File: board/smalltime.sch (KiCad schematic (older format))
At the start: 60 parts, among them IC1 STM32F030K6T6, IC2 MCP1700, IC3 DS3231MZ, J1 MICROUSB, P1 SWD, P2 SWD_TC, Q1 PFET, Q10 TEPT4400, Q2 PFET, Q3 PFET, Q4 PFET, Q5 PFET, Q6 PFET, Q7 PFET, Q8 PFET, Q9 PFET, SW1 INC, SW2 SET, U1 COM-09481, U2 COM-09481, X1 BATTERY

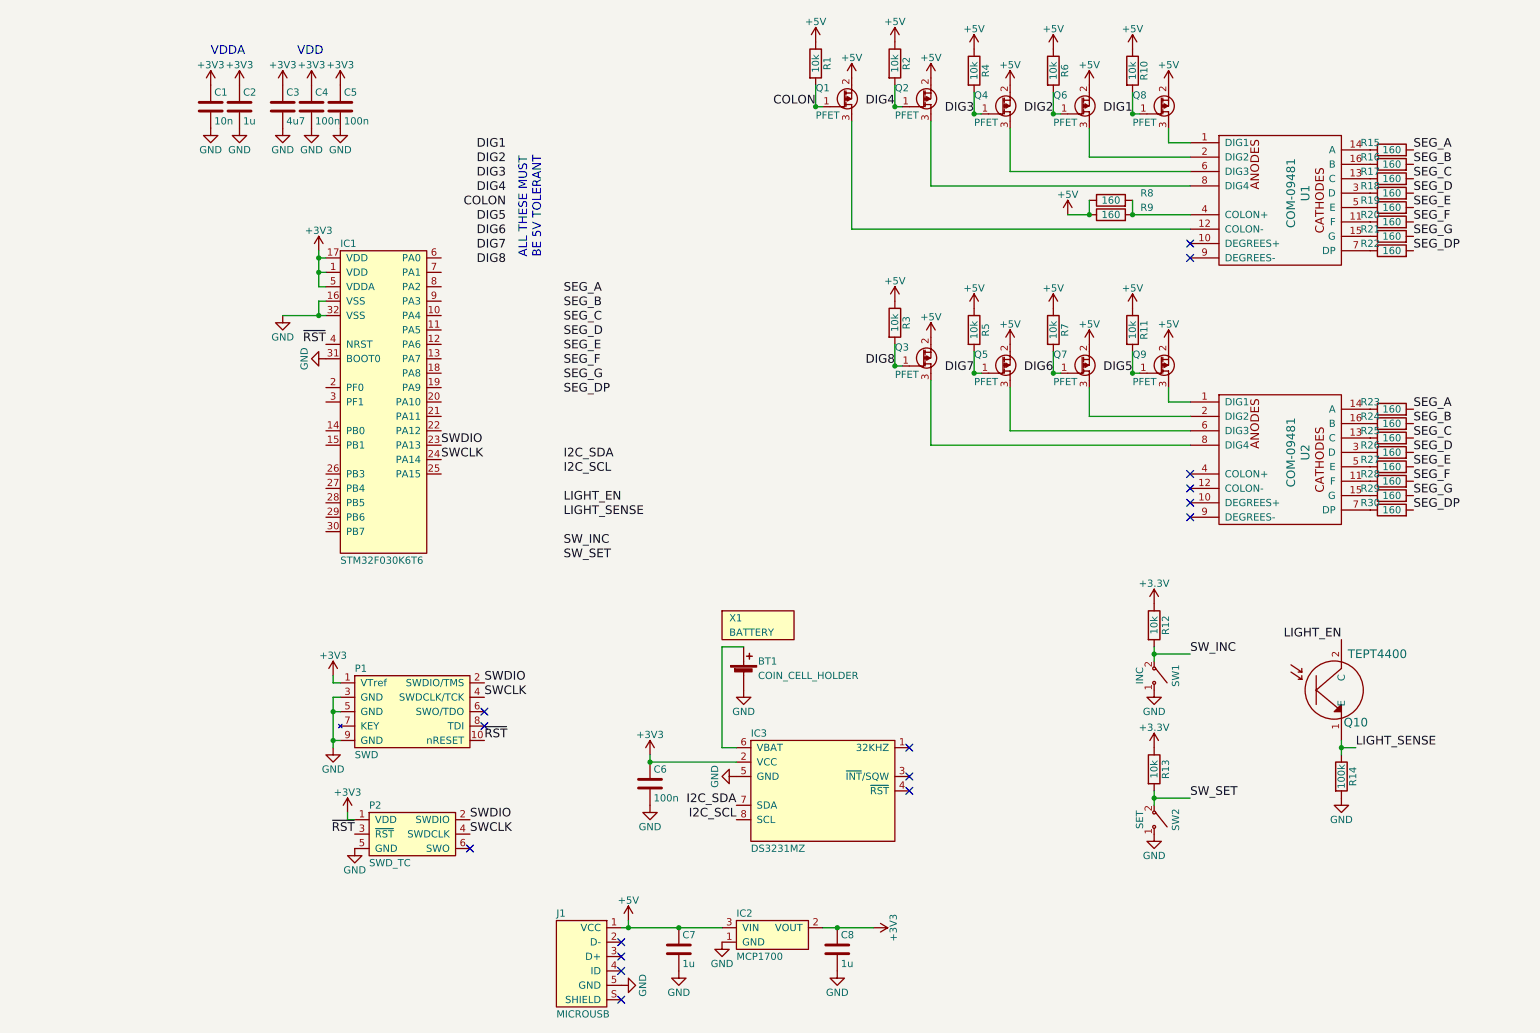
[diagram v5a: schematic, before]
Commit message: bigger 7segs, better LDO, NFETs, CR1220
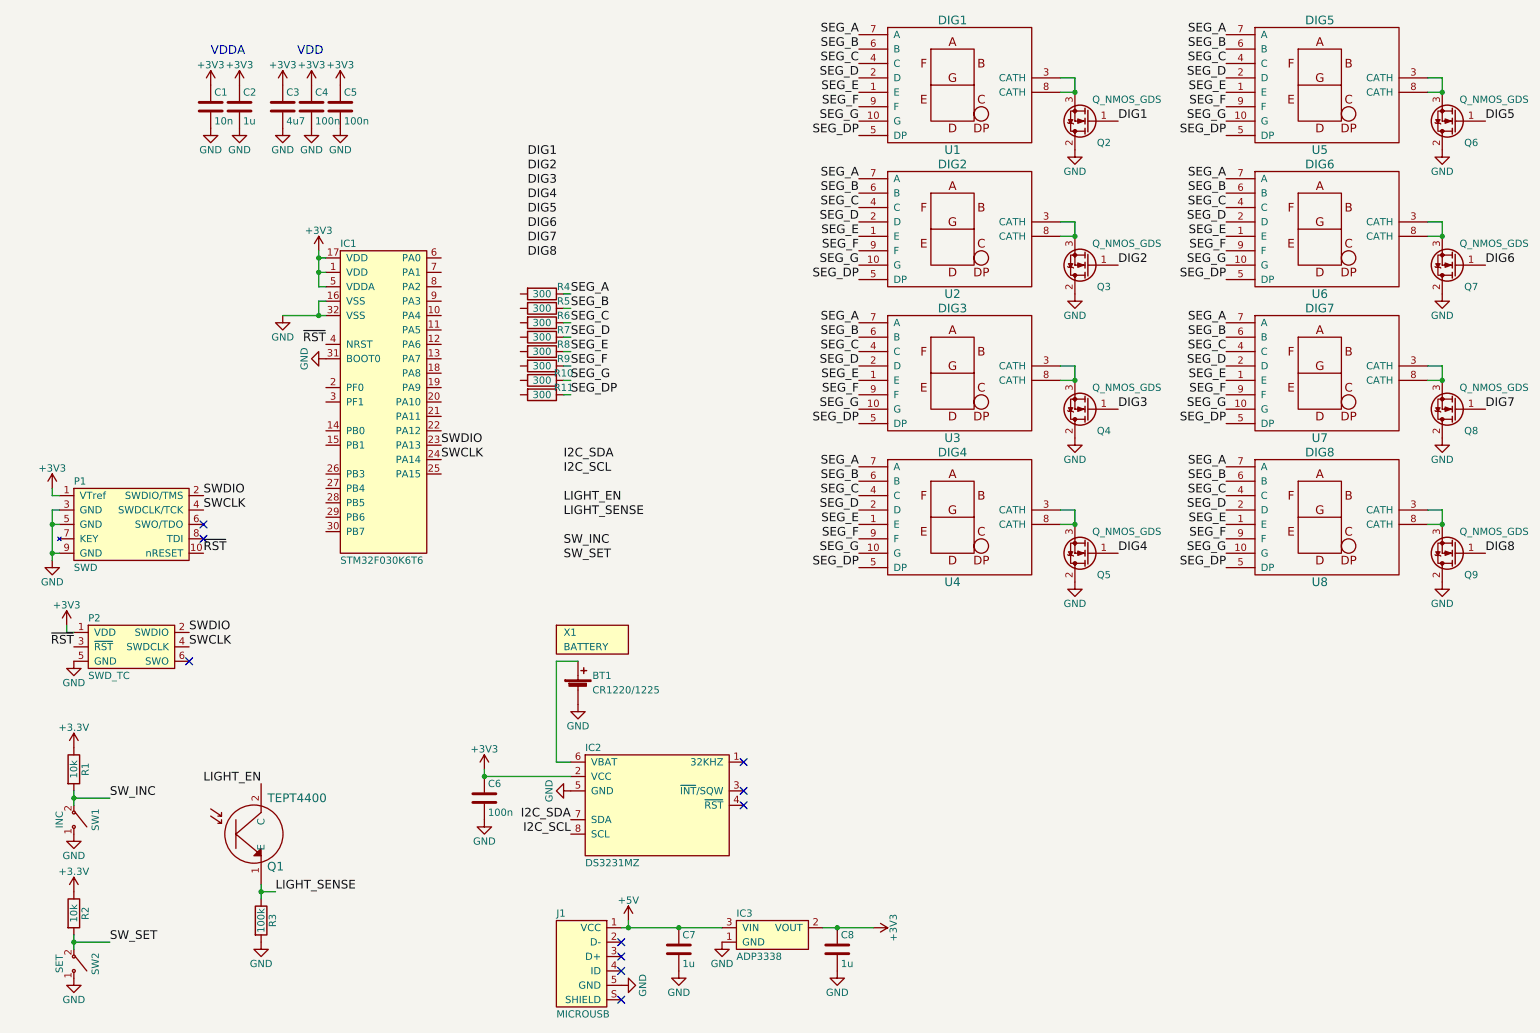
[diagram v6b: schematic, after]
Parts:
- removed IC2: MCP1700, agg:SOT-23, symbol MCP1700
- removed Q1, Q2, Q3, Q4, Q5, Q6, Q7, Q8, Q9: PFET, agg:SOT-23, symbol PFET
- removed R1, R2, R3: 10k, agg:0603, symbol R
- removed R15, R16, R17, R18, R19, R20, R21, R22, R23, R24, R25, R26, R27, R28, R29, R30: 160, agg:0603, symbol R
- removed U1, U2: COM-09481, smalltime:YSD-439AB4B-35, symbol COM-09481
- added IC3: ADP3338, agg-unchecked:SOT223, symbol ADP3338
- added Q2, Q3, Q4, Q5, Q6, Q7, Q8, Q9: Q_NMOS_GDS, agg:SOT-23, symbol Q_NMOS_GDS
- added U1: DIG1, smalltime:LS0803GWK, symbol LS0803GWK
- added U2: DIG2, smalltime:LS0803GWK, symbol LS0803GWK
- added U3: DIG3, smalltime:LS0803GWK, symbol LS0803GWK
- added U4: DIG4, smalltime:LS0803GWK, symbol LS0803GWK
- added U5: DIG5, smalltime:LS0803GWK, symbol LS0803GWK
- added U6: DIG6, smalltime:LS0803GWK, symbol LS0803GWK
- added U7: DIG7, smalltime:LS0803GWK, symbol LS0803GWK
- added U8: DIG8, smalltime:LS0803GWK, symbol LS0803GWK
- BT1: value COIN_CELL_HOLDER -> CR1220/1225; footprint smalltime:2032HOLDER_KS1060 -> smalltime:KEYSTONE500; Farnell 1704232 -> 3029839
- R10, R11, R4, R5, R6, R7: value 10k -> 300; Farnell 2447230 -> 2447331
- R8, R9: value 160 -> 300; Farnell 2447260 -> 2447331
- X1: Farnell 5219590 -> 4199091
- renumbered IC3 to IC2, Q10 to Q1, R12 to R1, R13 to R2, R14 to R3
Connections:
- net +3V3: now also IC3.2 (VOUT)
- net +5V: now also IC3.3 (VIN); no longer R10.1, R11.1, R4.1, R5.1, R6.1, R7.1, R8.1, R9.1
- net DIG1: now also Q2.1 (G); no longer R10.2
- net DIG2: now also Q3.1 (G); no longer R6.2
- net DIG3: now also Q4.1 (G); no longer R4.2
- net DIG4: now also Q5.1 (G)
- net DIG5: now also Q6.1 (G); no longer R11.2
- net DIG6: now also Q7.1 (G); no longer R7.2
- net DIG7: now also Q8.1 (G); no longer R5.2
- net DIG8: now also Q9.1 (G)
- net GND: now also IC3.1 (GND), Q2.2 (D), Q3.2 (D), Q4.2 (D), Q5.2 (D), Q6.2 (D), Q7.2 (D), Q8.2 (D), Q9.2 (D)
- net SEG_A: now also R4.1, U1.7 (A), U2.7 (A), U3.7 (A), U4.7 (A), U5.7 (A), U6.7 (A), U7.7 (A), U8.7 (A)
- net SEG_B: now also R5.1, U1.6 (B), U2.6 (B), U3.6 (B), U4.6 (B), U5.6 (B), U6.6 (B), U7.6 (B), U8.6 (B)
- net SEG_C: now also R6.1, U1.4 (C), U2.4 (C), U3.4 (C), U4.4 (C), U5.4 (C), U6.4 (C), U7.4 (C), U8.4 (C)
- net SEG_D: now also R7.1, U1.2 (D), U2.2 (D), U3.2 (D), U4.2 (D), U5.2 (D), U6.2 (D), U7.2 (D), U8.2 (D)
- net SEG_DP: now also R11.1, U1.5 (DP), U2.5 (DP), U3.5 (DP), U4.5 (DP), U5.5 (DP), U6.5 (DP), U7.5 (DP), U8.5 (DP)
- net SEG_E: now also R8.1, U1.1 (E), U2.1 (E), U3.1 (E), U4.1 (E), U5.1 (E), U6.1 (E), U7.1 (E), U8.1 (E)
- net SEG_F: now also R9.1, U1.9 (F), U2.9 (F), U3.9 (F), U4.9 (F), U5.9 (F), U6.9 (F), U7.9 (F), U8.9 (F)
- net SEG_G: now also R10.1, U1.10 (G), U2.10 (G), U3.10 (G), U4.10 (G), U5.10 (G), U6.10 (G), U7.10 (G), U8.10 (G)
- net at R8.2: no longer R9.2
- new net: Q3.3 (S), U2.3 (CATH), U2.8 (CATH)
- new net: Q4.3 (S), U3.3 (CATH), U3.8 (CATH)
- new net: Q5.3 (S), U4.3 (CATH), U4.8 (CATH)
- new net: Q6.3 (S), U5.3 (CATH), U5.8 (CATH)
- new net: Q7.3 (S), U6.3 (CATH), U6.8 (CATH)
- new net: Q8.3 (S), U7.3 (CATH), U7.8 (CATH)
- new net: Q9.3 (S), U8.3 (CATH), U8.8 (CATH)
- new net: Q2.3 (S), U1.3 (CATH), U1.8 (CATH)
- no-connect marks 16 -> 10
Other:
- note removed: "ALL THESE MUST\nBE 5V TOLERANT"
- moved on the sheet: BT1, C6, IC2, P1, P2, Q1, R1, R2, R3, SW1, SW2, X1

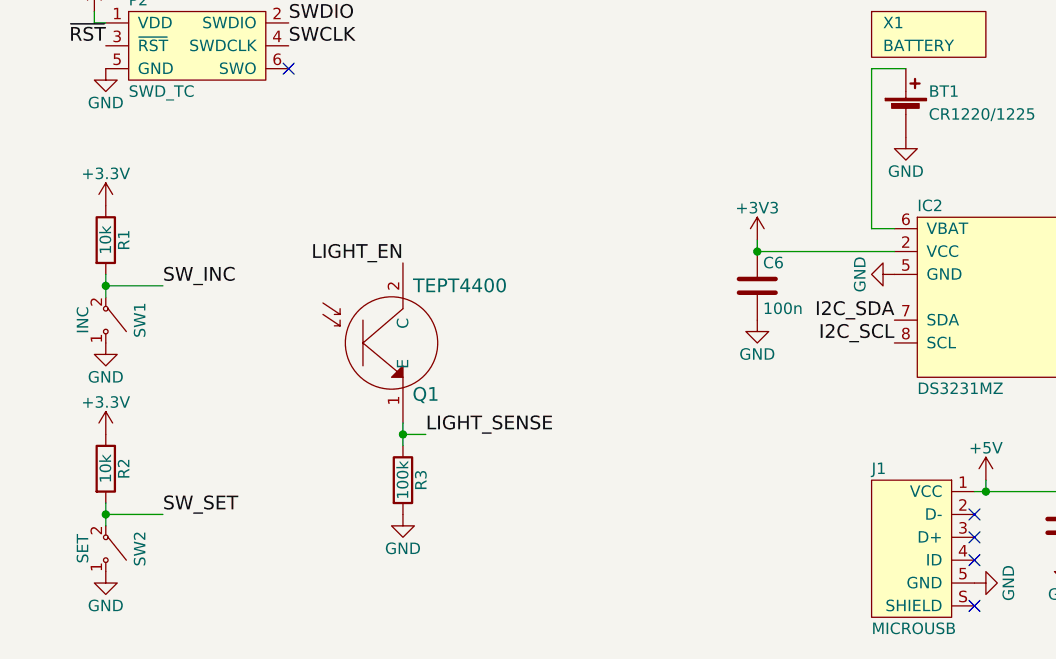
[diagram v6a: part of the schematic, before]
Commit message: removed unnecessary pullups
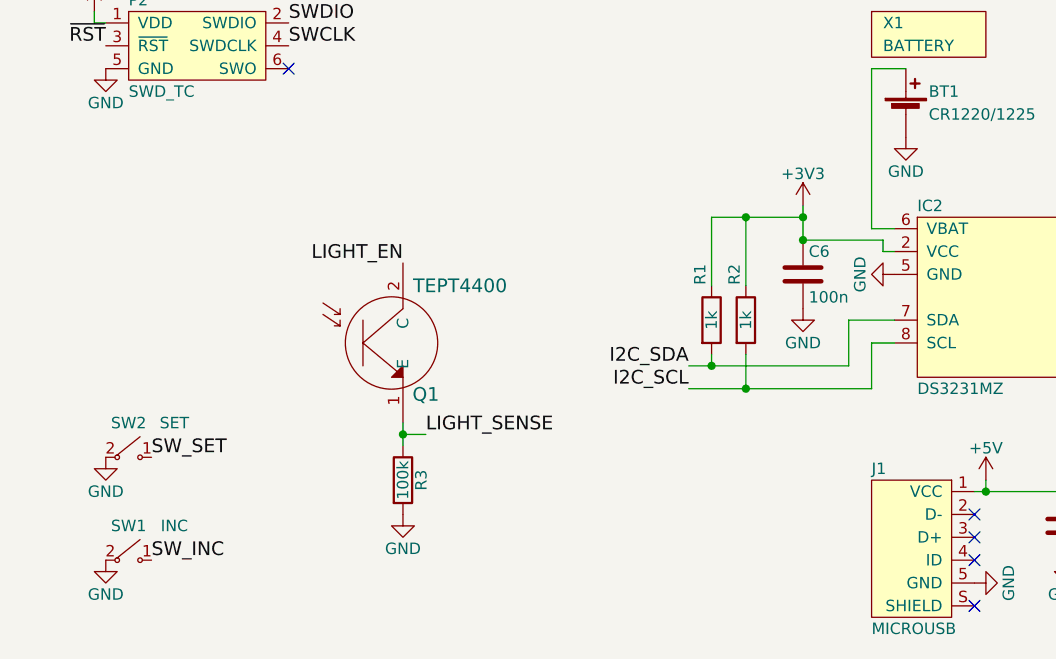
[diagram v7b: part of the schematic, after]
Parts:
- R1, R2: value 10k -> 1k; Farnell 2447230 -> (none)
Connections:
- net GND: now also SW1.2 ("~"), SW2.2 ("~"); no longer SW1.1 ("~"), SW2.1 ("~")
- net I2C_SCL: now also R2.2
- net I2C_SDA: now also R1.2
- net SW_INC: now also SW1.1 ("~"); no longer R1.2, SW1.2 ("~")
- net SW_SET: now also SW2.1 ("~"); no longer R2.2, SW2.2 ("~")
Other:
- moved on the sheet: C6, SW1, SW2
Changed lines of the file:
@@
 L +3V3 #PWR02
 U 1 1 59725FA1
-P 3750 5750
-F 0 "#PWR02" H 3750 5600 50  0001 C CNN
-F 1 "+3V3" H 3750 5890 50  0000 C CNN
-F 2 "" H 3750 5750 50  0001 C CNN
-F 3 "" H 3750 5750 50  0001 C CNN
-	1    3750 5750
-	1    0    0    -1
-$EndComp
-Wire Wire Line
-	3750 5750 3750 5800
-Wire Wire Line
-	3750 5800 4350 5800
-Connection ~ 3750 5800
+P 3950 5600
+F 0 "#PWR02" H 3950 5450 50  0001 C CNN
+F 1 "+3V3" H 3950 5740 50  0000 C CNN
+F 2 "" H 3950 5600 50  0001 C CNN
+F 3 "" H 3950 5600 50  0001 C CNN
+	1    3950 5600
+	1    0    0    -1
+$EndComp
+Wire Wire Line
+	3950 5600 3950 5750
+Connection ~ 3950 5750
 $Comp
 L GND #PWR03
 U 1 1 597260BD
-P 3750 6100
-F 0 "#PWR03" H 3750 5850 50  0001 C CNN
-F 1 "GND" H 3750 5950 50  0000 C CNN
-F 2 "" H 3750 6100 50  0001 C CNN
-F 3 "" H 3750 6100 50  0001 C CNN
-	1    3750 6100
+P 3950 6050
+F 0 "#PWR03" H 3950 5800 50  0001 C CNN
+F 1 "GND" H 3950 5900 50  0000 C CNN
+F 2 "" H 3950 6050 50  0001 C CNN
+F 3 "" H 3950 6050 50  0001 C CNN
+	1    3950 6050
 	1    0    0    -1
 $EndComp
@@
 	0    1    1    0
 $EndComp
-Text Label 4350 6100 2    60   ~ 0
+Text Label 3450 6300 2    60   ~ 0
 I2C_SDA
-Text Label 4350 6200 2    60   ~ 0
+Text Label 3450 6400 2    60   ~ 0
 I2C_SCL
 NoConn ~ 5550 5700
@@
 L SWITCH_SPST SW1
 U 1 1 5974012E
-P 900 6100
-F 0 "SW1" H 900 6250 50  0000 C CNN
-F 1 "INC" H 900 6000 50  0000 C CNN
-F 2 "smalltime:SKHHLSA010" H 900 6100 50  0001 C CNN
-F 3 "" H 900 6100 50  0001 C CNN
-F 4 "2056829" H 900 6100 60  0001 C CNN "Farnell"
-	1    900  6100
-	0    1    1    0
+P 1000 7150
+F 0 "SW1" H 1000 7300 50  0000 C CNN
+F 1 "INC" H 1200 7300 50  0000 C CNN
+F 2 "smalltime:SKHHLSA010" H 1000 7150 50  0001 C CNN
+F 3 "" H 1000 7150 50  0001 C CNN
+F 4 "2056829" H 1000 7150 60  0001 C CNN "Farnell"
+	1    1000 7150
+	1    0    0    -1
 $EndComp
 $Comp
 L SWITCH_SPST SW2
 U 1 1 59740C4F
-P 900 7100
-F 0 "SW2" H 900 7250 50  0000 C CNN
-F 1 "SET" H 900 7000 50  0000 C CNN
-F 2 "smalltime:SKHHLSA010" H 900 7100 50  0001 C CNN
-F 3 "" H 900 7100 50  0001 C CNN
-F 4 "2056829" H 900 7100 60  0001 C CNN "Farnell"
-	1    900  7100
-	0    1    1    0
+P 1000 6700
+F 0 "SW2" H 1000 6850 50  0000 C CNN
+F 1 "SET" H 1200 6850 50  0000 C CNN
+F 2 "smalltime:SKHHLSA010" H 1000 6700 50  0001 C CNN
+F 3 "" H 1000 6700 50  0001 C CNN
+F 4 "2056829" H 1000 6700 60  0001 C CNN "Farnell"
+	1    1000 6700
+	1    0    0    -1
 $EndComp
 $Comp
 L GND #PWR029
 U 1 1 59742178
-P 900 6200
-F 0 "#PWR029" H 900 5950 50  0001 C CNN
-F 1 "GND" H 900 6050 50  0000 C CNN
-F 2 "" H 900 6200 50  0001 C CNN
-F 3 "" H 900 6200 50  0001 C CNN
-	1    900  6200
-	1    0    0    -1
-$EndComp
-$Comp
-L R R1
-U 1 1 597426F4
-P 900 5750
-F 0 "R1" V 980 5750 50  0000 C CNN
-F 1 "10k" V 900 5750 50  0000 C CNN
-F 2 "agg:0603" V 830 5750 50  0001 C CNN
-F 3 "" H 900 5750 50  0001 C CNN
-F 4 "2447230" V 900 5750 60  0001 C CNN "Farnell"
-	1    900  5750
-	1    0    0    -1
-$EndComp
-Wire Wire Line
-	900  5900 900  6000
-Wire Wire Line
-	900  5950 1150 5950
-Connection ~ 900  5950
-Text Label 1150 5950 0    60   ~ 0
+P 900 7150
+F 0 "#PWR029" H 900 6900 50  0001 C CNN
+F 1 "GND" H 900 7000 50  0000 C CNN
+F 2 "" H 900 7150 50  0001 C CNN
+F 3 "" H 900 7150 50  0001 C CNN
+	1    900  7150
+	1    0    0    -1
+$EndComp
+Text Label 1100 7150 0    60   ~ 0
 SW_INC
 $Comp
-L +3.3V #PWR030
-U 1 1 597436C4
-P 900 5600
-F 0 "#PWR030" H 900 5450 50  0001 C CNN
-F 1 "+3.3V" H 900 5740 50  0000 C CNN
-F 2 "" H 900 5600 50  0001 C CNN
-F 3 "" H 900 5600 50  0001 C CNN
-	1    900  5600
-	1    0    0    -1
-$EndComp
-$Comp
-L R R2
-U 1 1 59745049
-P 900 6750
-F 0 "R2" V 980 6750 50  0000 C CNN
-F 1 "10k" V 900 6750 50  0000 C CNN
-F 2 "agg:0603" V 830 6750 50  0001 C CNN
-F 3 "" H 900 6750 50  0001 C CNN
-F 4 "2447230" V 900 6750 60  0001 C CNN "Farnell"
-	1    900  6750
-	1    0    0    -1
-$EndComp
-$Comp
-L +3.3V #PWR031
-U 1 1 59745174
-P 900 6600
-F 0 "#PWR031" H 900 6450 50  0001 C CNN
-F 1 "+3.3V" H 900 6740 50  0000 C CNN
-F 2 "" H 900 6600 50  0001 C CNN
-F 3 "" H 900 6600 50  0001 C CNN
-	1    900  6600
-	1    0    0    -1
-$EndComp
-$Comp
-L GND #PWR032
+L GND #PWR030
 U 1 1 597453E5
-P 900 7200
-F 0 "#PWR032" H 900 6950 50  0001 C CNN
-F 1 "GND" H 900 7050 50  0000 C CNN
-F 2 "" H 900 7200 50  0001 C CNN
-F 3 "" H 900 7200 50  0001 C CNN
-	1    900  7200
-	1    0    0    -1
-$EndComp
-Wire Wire Line
-	900  6900 900  7000
-Wire Wire Line
-	900  6950 1150 6950
-Connection ~ 900  6950
-Text Label 1150 6950 0    60   ~ 0
+P 900 6700
+F 0 "#PWR030" H 900 6450 50  0001 C CNN
+F 1 "GND" H 900 6550 50  0000 C CNN
+F 2 "" H 900 6700 50  0001 C CNN
+F 3 "" H 900 6700 50  0001 C CNN
+	1    900  6700
+	1    0    0    -1
+$EndComp
+Text Label 1100 6700 0    60   ~ 0
 SW_SET
 Text Label 4300 4200 0    60   ~ 0
@@
 L C C6
 U 1 1 597700C6
-P 3750 5950
-F 0 "C6" H 3775 6050 50  0000 L CNN
-F 1 "100n" H 3775 5850 50  0000 L CNN
-F 2 "agg:0603" H 3788 5800 50  0001 C CNN
-F 3 "" H 3750 5950 50  0001 C CNN
-F 4 "2627427" H 3750 5950 60  0001 C CNN "Farnell"
-	1    3750 5950
+P 3950 5900
+F 0 "C6" H 3975 6000 50  0000 L CNN
+F 1 "100n" H 3975 5800 50  0000 L CNN
+F 2 "agg:0603" H 3988 5750 50  0001 C CNN
+F 3 "" H 3950 5900 50  0001 C CNN
+F 4 "2627427" H 3950 5900 60  0001 C CNN "Farnell"
+	1    3950 5900
 	1    0    0    -1
 $EndComp
@@
 Connection ~ 7850 1050
 $Comp
-L GND #PWR033
+L GND #PWR031
 U 1 1 59794EE7
 P 7850 1450
-F 0 "#PWR033" H 7850 1200 50  0001 C CNN
+F 0 "#PWR031" H 7850 1200 50  0001 C CNN
 F 1 "GND" H 7850 1300 50  0000 C CNN
 F 2 "" H 7850 1450 50  0001 C CNN
@@
 Connection ~ 10400 1050
 $Comp
-L GND #PWR034
+L GND #PWR032
 U 1 1 5979C4E1
 P 10400 1450
-F 0 "#PWR034" H 10400 1200 50  0001 C CNN
+F 0 "#PWR032" H 10400 1200 50  0001 C CNN
 F 1 "GND" H 10400 1300 50  0000 C CNN
 F 2 "" H 10400 1450 50  0001 C CNN
@@
 Connection ~ 7850 2050
 $Comp
-L GND #PWR035
+L GND #PWR033
 U 1 1 5979C6FD
 P 7850 2450
-F 0 "#PWR035" H 7850 2200 50  0001 C CNN
+F 0 "#PWR033" H 7850 2200 50  0001 C CNN
 F 1 "GND" H 7850 2300 50  0000 C CNN
 F 2 "" H 7850 2450 50  0001 C CNN
@@
 Connection ~ 10400 2050
 $Comp
-L GND #PWR036
+L GND #PWR034
 U 1 1 5979C71D
 P 10400 2450
-F 0 "#PWR036" H 10400 2200 50  0001 C CNN
+F 0 "#PWR034" H 10400 2200 50  0001 C CNN
 F 1 "GND" H 10400 2300 50  0000 C CNN
 F 2 "" H 10400 2450 50  0001 C CNN
@@
 Connection ~ 7850 3050
 $Comp
-L GND #PWR037
+L GND #PWR035
 U 1 1 5979F277
 P 7850 3450
-F 0 "#PWR037" H 7850 3200 50  0001 C CNN
+F 0 "#PWR035" H 7850 3200 50  0001 C CNN
 F 1 "GND" H 7850 3300 50  0000 C CNN
 F 2 "" H 7850 3450 50  0001 C CNN
@@
 Connection ~ 10400 3050
 $Comp
-L GND #PWR038
+L GND #PWR036
 U 1 1 5979F297
 P 10400 3450
-F 0 "#PWR038" H 10400 3200 50  0001 C CNN
+F 0 "#PWR036" H 10400 3200 50  0001 C CNN
 F 1 "GND" H 10400 3300 50  0000 C CNN
 F 2 "" H 10400 3450 50  0001 C CNN
@@
 Connection ~ 7850 4050
 $Comp
-L GND #PWR039
+L GND #PWR037
 U 1 1 5979F2B7
 P 7850 4450
-F 0 "#PWR039" H 7850 4200 50  0001 C CNN
+F 0 "#PWR037" H 7850 4200 50  0001 C CNN
 F 1 "GND" H 7850 4300 50  0000 C CNN
 F 2 "" H 7850 4450 50  0001 C CNN
@@
 Connection ~ 10400 4050
 $Comp
-L GND #PWR040
+L GND #PWR038
 U 1 1 5979F2D7
 P 10400 4450
-F 0 "#PWR040" H 10400 4200 50  0001 C CNN
+F 0 "#PWR038" H 10400 4200 50  0001 C CNN
 F 1 "GND" H 10400 4300 50  0000 C CNN
 F 2 "" H 10400 4450 50  0001 C CNN
@@
 	1    0    0    -1
 $EndComp
+$Comp
+L R R2
+U 1 1 5979E859
+P 3700 6100
+F 0 "R2" V 3650 6300 50  0000 C CNN
+F 1 "1k" V 3700 6100 50  0000 C CNN
+F 2 "agg:0603" V 3630 6100 50  0001 C CNN
+F 3 "" H 3700 6100 50  0001 C CNN
+	1    3700 6100
+	1    0    0    -1
+$EndComp
+$Comp
+L R R1
+U 1 1 597A069D
+P 3550 6100
+F 0 "R1" V 3500 6300 50  0000 C CNN
+F 1 "1k" V 3550 6100 50  0000 C CNN
+F 2 "agg:0603" V 3480 6100 50  0001 C CNN
+F 3 "" H 3550 6100 50  0001 C CNN
+	1    3550 6100
+	1    0    0    -1
+$EndComp
+Wire Wire Line
+	4300 5750 4300 5800
+Wire Wire Line
+	4300 5800 4350 5800
+Wire Wire Line
+	3950 5750 4300 5750
+Wire Wire Line
+	3450 6300 4150 6300
+Wire Wire Line
+	4150 6300 4150 6100
+Wire Wire Line
+	4150 6100 4350 6100
+Wire Wire Line
+	4350 6200 4250 6200
+Wire Wire Line
+	4250 6200 4250 6400
+Wire Wire Line
+	4250 6400 3450 6400
+Wire Wire Line
+	3550 6250 3550 6300
+Connection ~ 3550 6300
+Wire Wire Line
+	3700 6250 3700 6400
+Connection ~ 3700 6400
+Wire Wire Line
+	3550 5950 3550 5650
+Wire Wire Line
+	3550 5650 3950 5650
+Connection ~ 3950 5650
+Wire Wire Line
+	3700 5950 3700 5650
+Connection ~ 3700 5650
 $EndSCHEMATC
